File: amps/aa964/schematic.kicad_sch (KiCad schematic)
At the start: 69 parts, among them SW1 AC sw, SW2 gnd sw

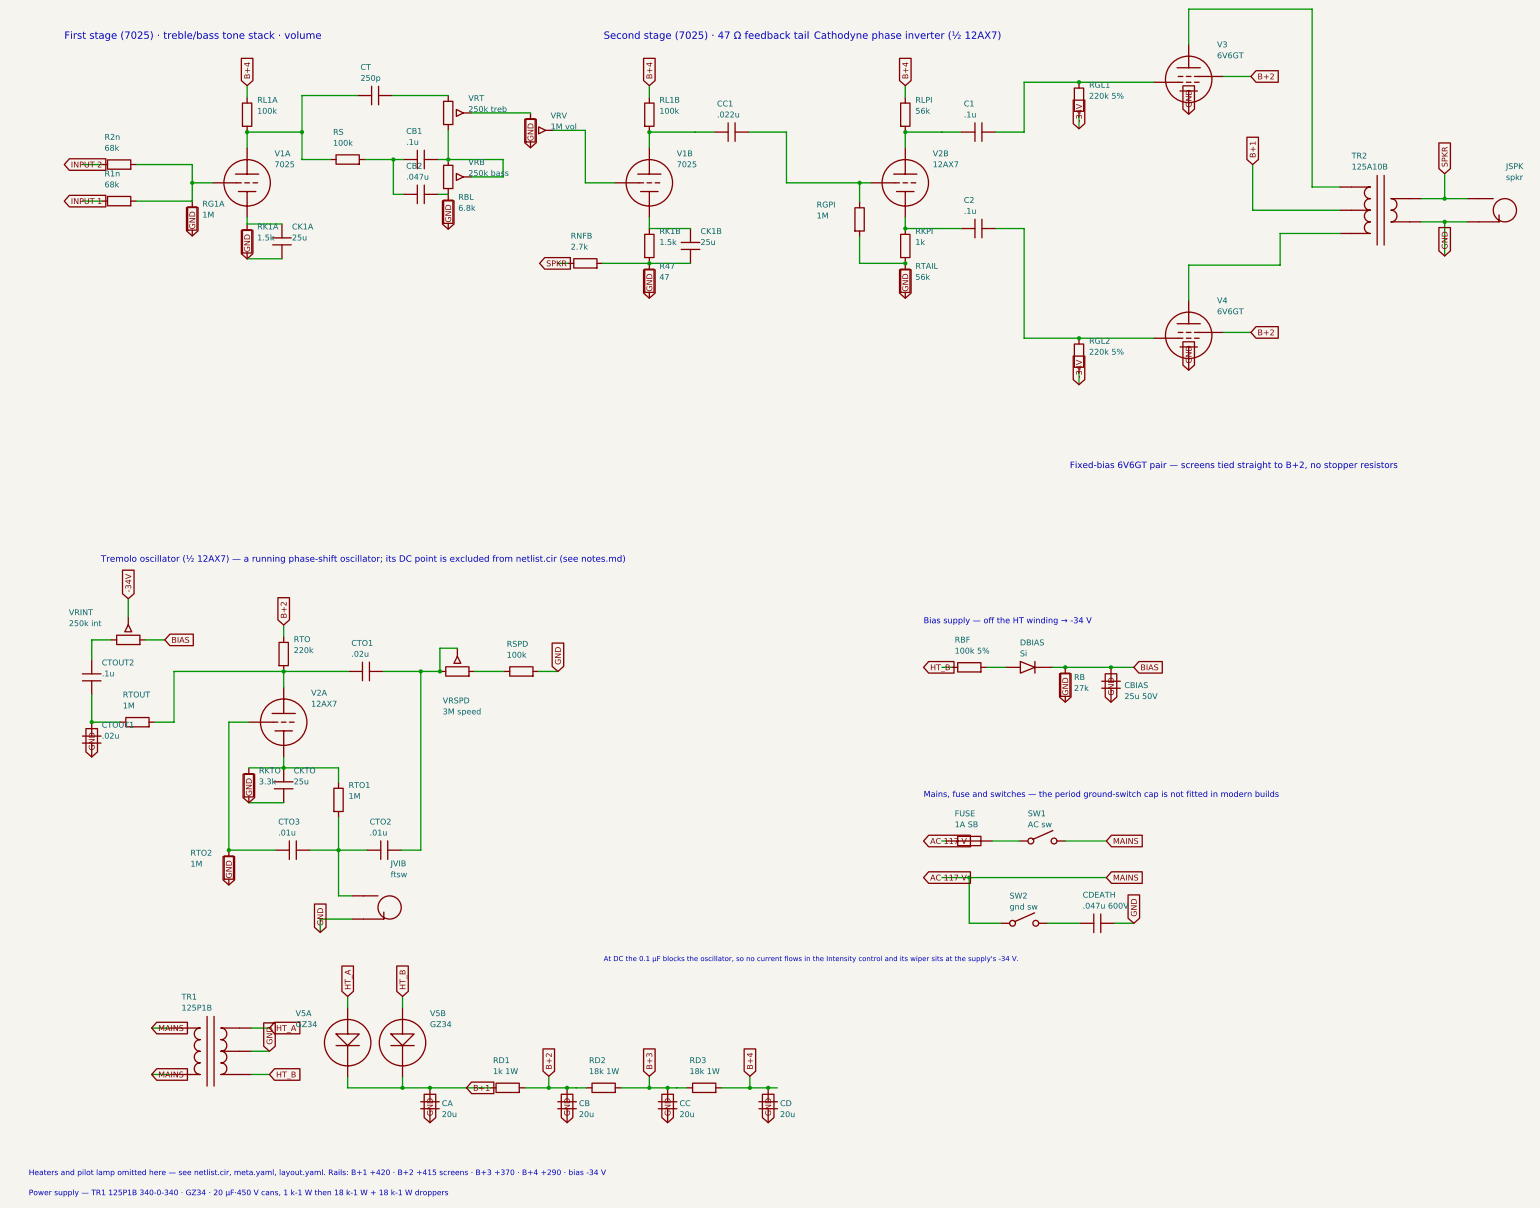
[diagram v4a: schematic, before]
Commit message: Fix: rotated global labels lettered their net names outside the flag
Every global label this pipeline emitted carried (justify left) regardless of
rotation. KiCanvas — like KiCad — draws label text horizontally at 0/180 and
vertically at 90/270 and reads WHICH SIDE of the anchor it letters on from the
justification, so at 180 and 270 the name printed outside an empty flag
outline, struck through by the very wire it names: 219 labels at 180 deg
(including the input-jack flags at top-left of nearly every sheet, the first
glyphs a visitor reads) and 792 GND/rail flags at 270 whose names squeezed at
the flag mouth instead of lettering down the body. The library already
compensated rotation for property text (`pa`); this mirrors that logic for
global labels: justify right at 180/270, left at 0/90.

check_schematics gains the geometry clause whose absence let all 1011
instances through a "no lettering through circuitry" pass: it modelled the
flag box but never the label TEXT, so a name rendered on the wrong side was
invisible to it. The gate now proves justification compensates rotation on
every global label.

Two more things this exposed, fixed in the same engine pass:

- Placement now measures with the renderer's own Newstroke advance table
  (extracted from the vendored kicanvas.js) instead of a flat 0.68-em prose
  average that under-read part lettering by a quarter — the mechanism behind
  every "metered clean, printed through its neighbour" incident. The GATE
  deliberately keeps the coarse ruler: re-ruling it with renderer truth was
  tried and red-flagged 28 of 34 sheets over abutments three visual passes
  had already judged sub-visual (the two-rulers note in schematic_lib.py).
- place_captions' escape ladder runs further, because a banner caption
  measured truly is half again wider than the old estimate believed.

All 34 schematics regenerated; full gate suite green.

🤖 Generated with [Claude Code](https://claude.com/claude-code)

Co-Authored-By: Claude Fable 5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
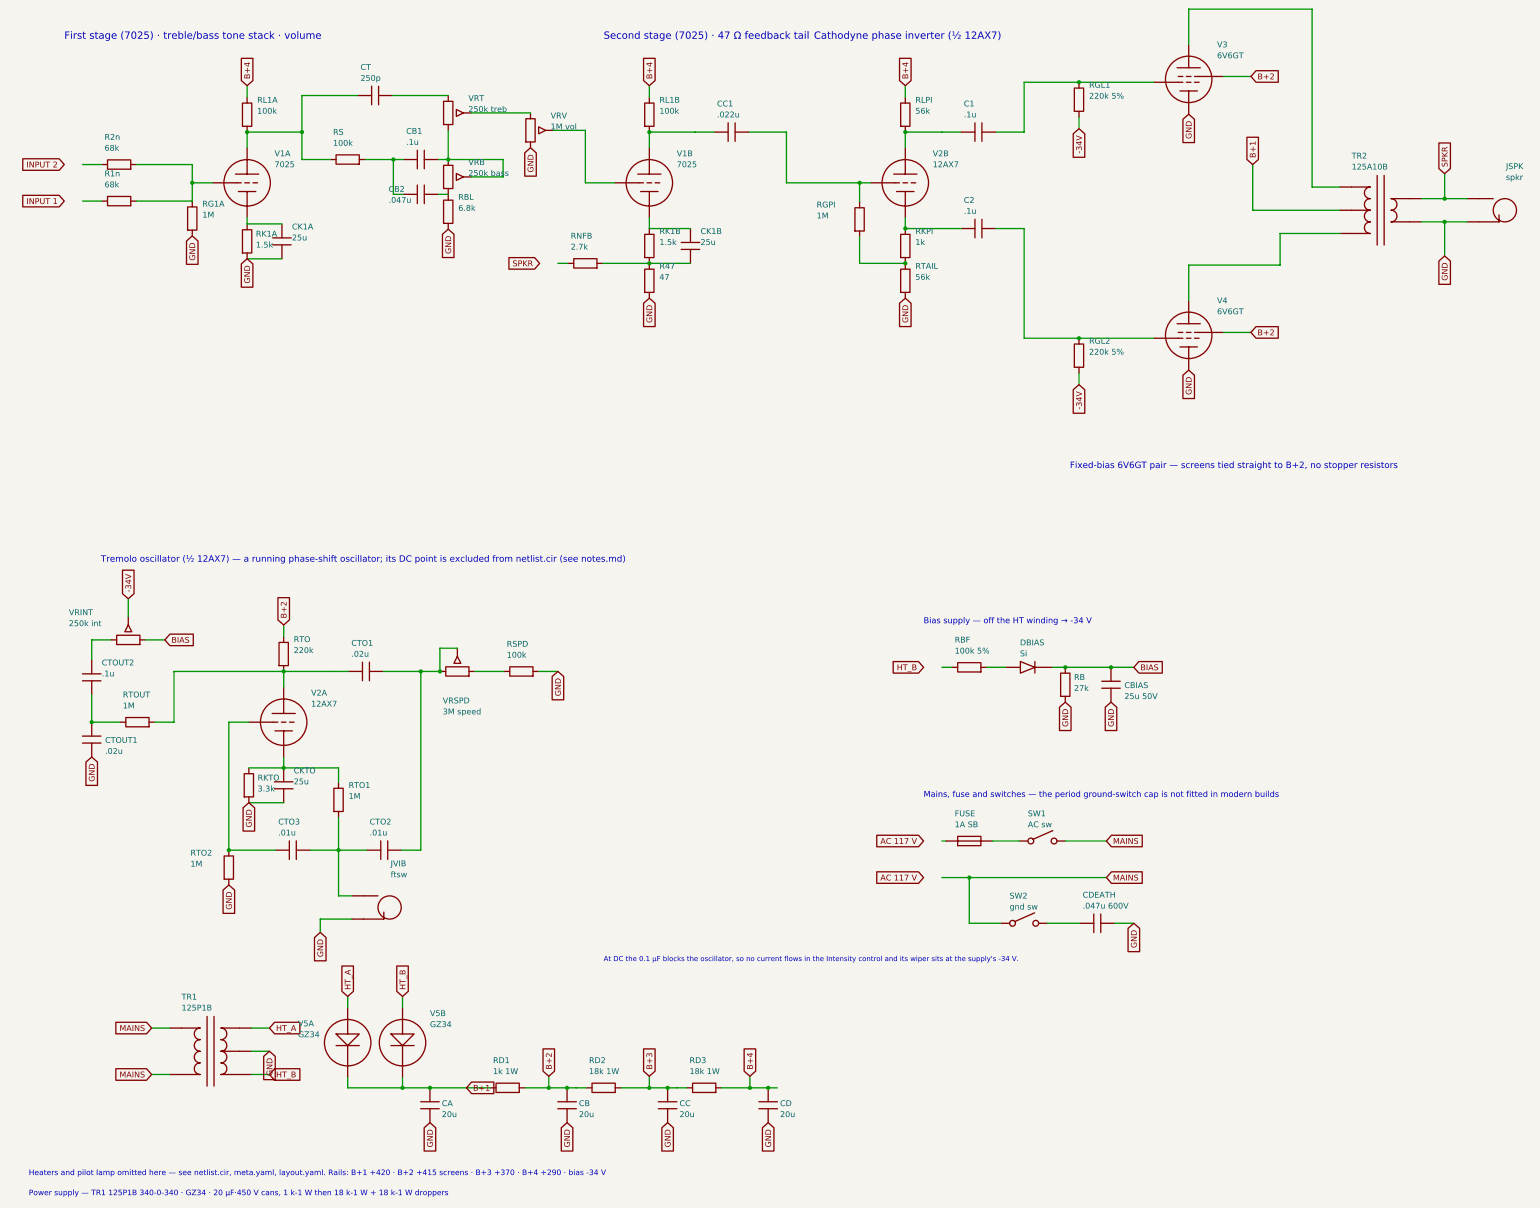
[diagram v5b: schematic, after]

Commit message: Fix: deterministic schematic ids and wires split at every join
- _u() is uuid5 over (amp id, emission order), so a regeneration of an
  unchanged script is byte-identical and a drift gate becomes possible
- write() splits wire segments at symbol pins, wire ends and junction dots,
  so the file connects exactly what the drawing shows under KiCad's
  endpoint-only semantics (270 pins were on a wire's interior; net
  partitions unchanged on all 38 sheets)
- all sheets regenerated; aa864-bassman title block was stale (draft) and
  now matches meta.yaml (verified)

Co-Authored-By: Claude Fable 5.1 <noreply@anthropic.com>
Claude-Session: https://claude.ai/code/session_01KBMfdh37HmCL2iWcBiL5J1
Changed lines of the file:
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@@
   (wire (pts (xy 36.2824 54.7) (xy 48.4724 54.7))
     (stroke (width 0) (type default)))
-  (wire (pts (xy 48.4724 46.7) (xy 48.4724 54.7))
+  (wire (pts (xy 48.4724 46.7) (xy 48.4724 50.7))
+    (stroke (width 0) (type default)))
+  (wire (pts (xy 48.4724 50.7) (xy 48.4724 54.7))
     (stroke (width 0) (type default)))
   (junction (at 48.4724 50.7) (diameter 0) (color 0 0 0 0))
@@
     (property "Reference" "V2B" (at 210.472 44.3 0) (effects (font (size 1.27 1.27)) (justify left)))
     (property "Value" "12AX7" (at 210.472 46.7 0) (effects (font (size 1.27 1.27)) (justify left))))
-  (wire (pts (xy 178.472 50.7) (xy 196.852 50.7))
+  (wire (pts (xy 178.472 50.7) (xy 194.472 50.7))
+    (stroke (width 0) (type default)))
+  (wire (pts (xy 194.472 50.7) (xy 196.852 50.7))
     (stroke (width 0) (type default)))
   (junction (at 194.472 50.7) (diameter 0) (color 0 0 0 0))
@@
     (property "Reference" "JSPK" (at 335.872 47.1 0) (effects (font (size 1.27 1.27)) (justify left)))
     (property "Value" "spkr" (at 335.872 49.5 0) (effects (font (size 1.27 1.27)) (justify left))))
-  (wire (pts (xy 317.362 54.16) (xy 327.392 54.16))
+  (wire (pts (xy 317.362 54.16) (xy 322.472 54.16))
+    (stroke (width 0) (type default)))
+  (wire (pts (xy 322.472 54.16) (xy 327.392 54.16))
     (stroke (width 0) (type default)))
   (junction (at 322.472 54.16) (diameter 0) (color 0 0 0 0))
@@
   (wire (pts (xy 322.472 48.7) (xy 322.472 54.16))
     (stroke (width 0) (type default)))
-  (wire (pts (xy 317.362 59.24) (xy 327.392 59.24))
+  (wire (pts (xy 317.362 59.24) (xy 322.472 59.24))
+    (stroke (width 0) (type default)))
+  (wire (pts (xy 322.472 59.24) (xy 327.392 59.24))
     (stroke (width 0) (type default)))
   (junction (at 322.472 59.24) (diameter 0) (color 0 0 0 0))
@@
   (wire (pts (xy 94.4724 246.44) (xy 94.4724 248.7))
     (stroke (width 0) (type default)))
-  (wire (pts (xy 82.4724 248.7) (xy 108.472 248.7))
+  (wire (pts (xy 82.4724 248.7) (xy 94.4724 248.7))
+    (stroke (width 0) (type default)))
+  (wire (pts (xy 94.4724 248.7) (xy 100.472 248.7))
+    (stroke (width 0) (type default)))
+  (wire (pts (xy 100.472 248.7) (xy 108.472 248.7))
     (stroke (width 0) (type default)))
   (junction (at 94.4724 248.7) (diameter 0) (color 0 0 0 0))
@@
   (wire (pts (xy 111.472 248.7) (xy 113.662 248.7))
     (stroke (width 0) (type default)))
-  (wire (pts (xy 121.282 248.7) (xy 132.472 248.7))
+  (wire (pts (xy 121.282 248.7) (xy 126.472 248.7))
+    (stroke (width 0) (type default)))
+  (wire (pts (xy 126.472 248.7) (xy 130.472 248.7))
+    (stroke (width 0) (type default)))
+  (wire (pts (xy 130.472 248.7) (xy 132.472 248.7))
     (stroke (width 0) (type default)))
   (junction (at 126.472 248.7) (diameter 0) (color 0 0 0 0))
@@
   (wire (pts (xy 132.472 248.7) (xy 134.662 248.7))
     (stroke (width 0) (type default)))
-  (wire (pts (xy 142.282 248.7) (xy 154.472 248.7))
+  (wire (pts (xy 142.282 248.7) (xy 148.472 248.7))
+    (stroke (width 0) (type default)))
+  (wire (pts (xy 148.472 248.7) (xy 152.472 248.7))
+    (stroke (width 0) (type default)))
+  (wire (pts (xy 152.472 248.7) (xy 154.472 248.7))
     (stroke (width 0) (type default)))
   (junction (at 148.472 248.7) (diameter 0) (color 0 0 0 0))
@@
   (wire (pts (xy 154.472 248.7) (xy 156.662 248.7))
     (stroke (width 0) (type default)))
-  (wire (pts (xy 164.282 248.7) (xy 176.472 248.7))
+  (wire (pts (xy 164.282 248.7) (xy 170.472 248.7))
+    (stroke (width 0) (type default)))
+  (wire (pts (xy 170.472 248.7) (xy 174.472 248.7))
+    (stroke (width 0) (type default)))
+  (wire (pts (xy 174.472 248.7) (xy 176.472 248.7))
     (stroke (width 0) (type default)))
   (junction (at 170.472 248.7) (diameter 0) (color 0 0 0 0))
@@
     (property "Reference" "DBIAS" (at 229.552 151.3 0) (effects (font (size 1.27 1.27)) (justify left)))
     (property "Value" "Si" (at 229.552 153.7 0) (effects (font (size 1.27 1.27)) (justify left))))
-  (wire (pts (xy 236.632 156.7) (xy 254.472 156.7))
+  (wire (pts (xy 236.632 156.7) (xy 239.472 156.7))
+    (stroke (width 0) (type default)))
+  (wire (pts (xy 239.472 156.7) (xy 249.472 156.7))
+    (stroke (width 0) (type default)))
+  (wire (pts (xy 249.472 156.7) (xy 254.472 156.7))
     (stroke (width 0) (type default)))
   (junction (at 239.472 156.7) (diameter 0) (color 0 0 0 0))
@@
   (global_label "AC 117 V" (shape input) (at 208.472 202.7 180)
     (effects (font (size 1.27 1.27)) (justify right)))
-  (wire (pts (xy 212.472 202.7) (xy 248.472 202.7))
+  (wire (pts (xy 212.472 202.7) (xy 218.472 202.7))
+    (stroke (width 0) (type default)))
+  (wire (pts (xy 218.472 202.7) (xy 248.472 202.7))
     (stroke (width 0) (type default)))
   (global_label "MAINS" (shape input) (at 248.472 202.7 0)

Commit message: Fix: schematic wiring on m1987, aa864-bassman, ac30, m1959, ga40, aa1164, aa964
- 58 open pins closed: leads that stopped short of their flags, pins
  missed by 0.01-0.11 mm, snubbers and bright caps with no leads
- two shorts the isolated-pin check cannot see: aa864-bassman V6 anode
  lead ran through its grounded cathode (plate rail to chassis) and its V5
  coupler drop shorted RGL1; m1987 RB1/RB2 stood on the wire they bridge
- 14 dated waivers: m1959 C29-C31 (factory sheet prints them unconnected),
  ga40 V2/V3/VR3.3 (net_map excluded tubes, free rheostat lug)
- all seven sheets pass connectivity and verify_schematic_nets

Co-Authored-By: Claude Fable 5.1 <noreply@anthropic.com>
Claude-Session: https://claude.ai/code/session_01KBMfdh37HmCL2iWcBiL5J1
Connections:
- net MAINS is gone; now on net AC 117 V: SW1.2, SW2.1, TR1.1 (PRI_1), TR1.2 (PRI_2)
- net AC 117 V: now also FUSE.1
- net HT_B: now also RBF.1
- net INPUT 1: now also R1n.1
- net INPUT 2: now also R2n.1
- net SPKR: now also RNFB.1
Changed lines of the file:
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@@
     (property "Reference" "R2n" (at 29.2724 40.7 270) (effects (font (size 1.27 1.27)) (justify left)))
     (property "Value" "68k" (at 29.2724 43.1 270) (effects (font (size 1.27 1.27)) (justify left))))
-  (wire (pts (xy 24.4724 46.7) (xy 28.6624 46.7))
+  (wire (pts (xy 20.4724 46.7) (xy 28.6624 46.7))
     (stroke (width 0) (type default)))
   (wire (pts (xy 36.2824 46.7) (xy 48.4724 46.7))
@@
     (property "Reference" "R1n" (at 29.2724 48.7 270) (effects (font (size 1.27 1.27)) (justify left)))
     (property "Value" "68k" (at 29.2724 51.1 270) (effects (font (size 1.27 1.27)) (justify left))))
-  (wire (pts (xy 24.4724 54.7) (xy 28.6624 54.7))
+  (wire (pts (xy 20.4724 54.7) (xy 28.6624 54.7))
     (stroke (width 0) (type default)))
   (wire (pts (xy 36.2824 54.7) (xy 48.4724 54.7))
@@
     (property "Reference" "RNFB" (at 131.272 62.32 270) (effects (font (size 1.27 1.27)) (justify left)))
     (property "Value" "2.7k" (at 131.272 64.72 270) (effects (font (size 1.27 1.27)) (justify left))))
-  (wire (pts (xy 128.472 68.32) (xy 130.662 68.32))
+  (wire (pts (xy 124.472 68.32) (xy 130.662 68.32))
     (stroke (width 0) (type default)))
   (wire (pts (xy 138.282 68.32) (xy 148.472 68.32))
@@
   (wire (pts (xy 170.472 248.7) (xy 174.472 248.7))
     (stroke (width 0) (type default)))
-  (wire (pts (xy 174.472 248.7) (xy 176.472 248.7))
-    (stroke (width 0) (type default)))
   (junction (at 170.472 248.7) (diameter 0) (color 0 0 0 0))
   (global_label "B+4" (shape input) (at 170.472 246.16 90)
@@
   (global_label "HT_B" (shape input) (at 208.472 156.7 180)
     (effects (font (size 1.27 1.27)) (justify right)))
-  (wire (pts (xy 212.472 156.7) (xy 214.662 156.7))
+  (wire (pts (xy 208.472 156.7) (xy 214.662 156.7))
     (stroke (width 0) (type default)))
   (symbol (lib_id "cx:R") (at 218.472 156.7 90) (unit 1)
@@
   (global_label "AC 117 V" (shape input) (at 208.472 194.7 180)
     (effects (font (size 1.27 1.27)) (justify right)))
-  (wire (pts (xy 212.472 194.7) (xy 213.392 194.7))
+  (wire (pts (xy 208.472 194.7) (xy 213.392 194.7))
     (stroke (width 0) (type default)))
   (symbol (lib_id "cx:FUSE") (at 218.472 194.7 0) (unit 1)
@@
   (global_label "AC 117 V" (shape input) (at 208.472 202.7 180)
     (effects (font (size 1.27 1.27)) (justify right)))
-  (wire (pts (xy 212.472 202.7) (xy 218.472 202.7))
+  (wire (pts (xy 208.472 202.7) (xy 218.472 202.7))
     (stroke (width 0) (type default)))
   (wire (pts (xy 218.472 202.7) (xy 248.472 202.7))
